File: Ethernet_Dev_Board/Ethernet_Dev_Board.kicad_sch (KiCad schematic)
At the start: 33 parts, among them J101 Power In, U101 AZ1117, U102 74AUP1T08GWH, U103 1.2V

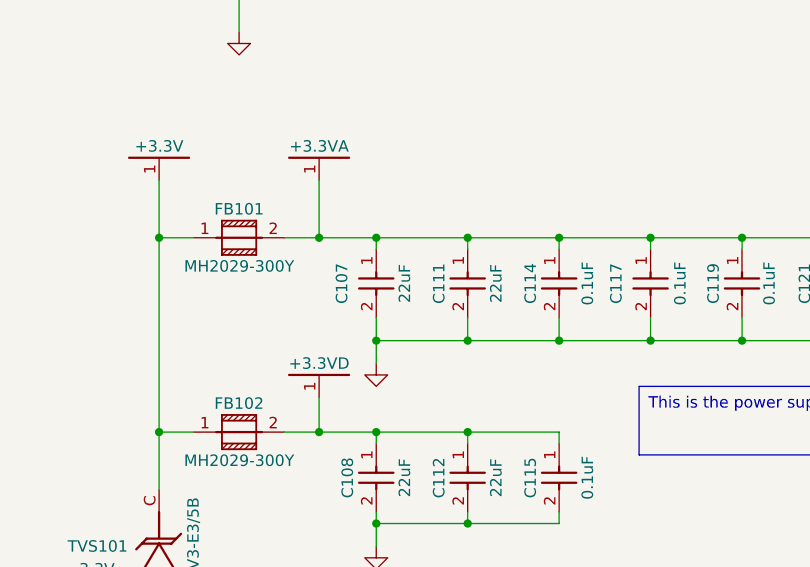
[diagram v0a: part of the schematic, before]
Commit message: Changed cap value to 2.2 and changed SS pin
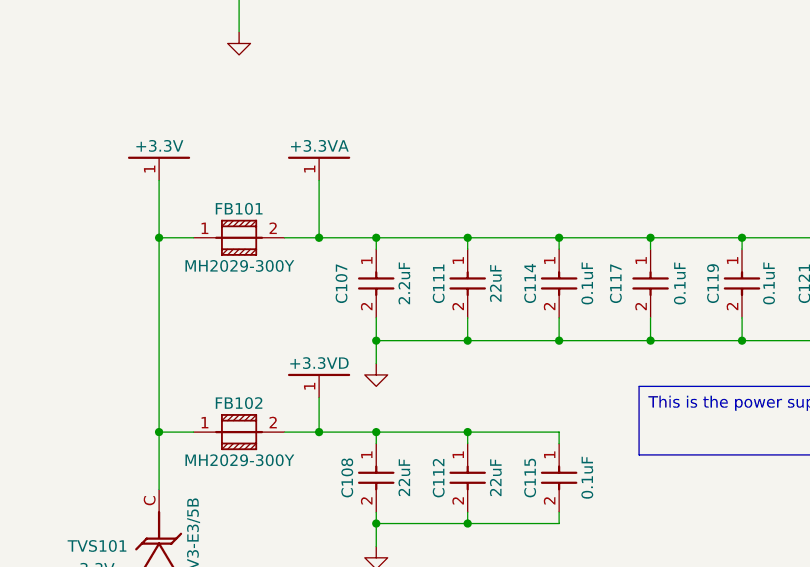
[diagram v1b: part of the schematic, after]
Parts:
- C107: value 22uF -> 2.2uF
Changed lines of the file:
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@@
 			)
 		)
-		(property "Value" "22uF"
+		(property "Value" "2.2uF"
 			(at 92.075 82.55 90)
 			(effects
